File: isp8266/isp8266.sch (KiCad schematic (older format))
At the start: 61 parts, among them J1 S0, J10 F1, J2 S2, J3 S1, J4 S3, J5 IMU, J6 USART, J7 F0, J8 BATTERY, J9 I2C, Q1 S8050, Q2 S8050, Q3 IRLML0030, Q4 IRLML0030, SW1 SW_Push, U1 CH340C, U2 AP1117-33, U3 IPS5306, U4 ESP-12E

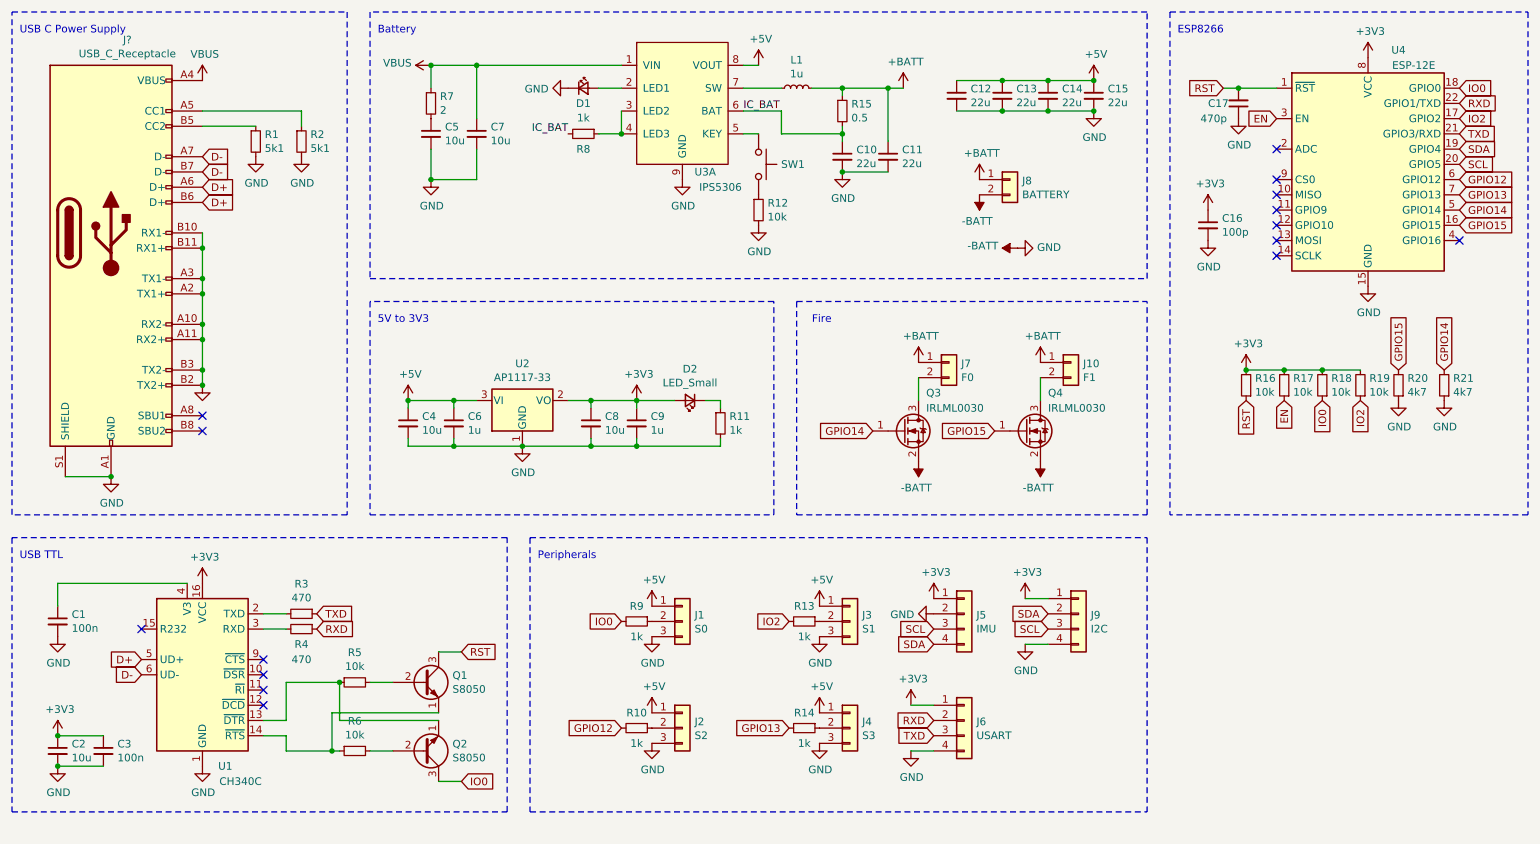
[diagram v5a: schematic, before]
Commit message: Add rst button and footprint
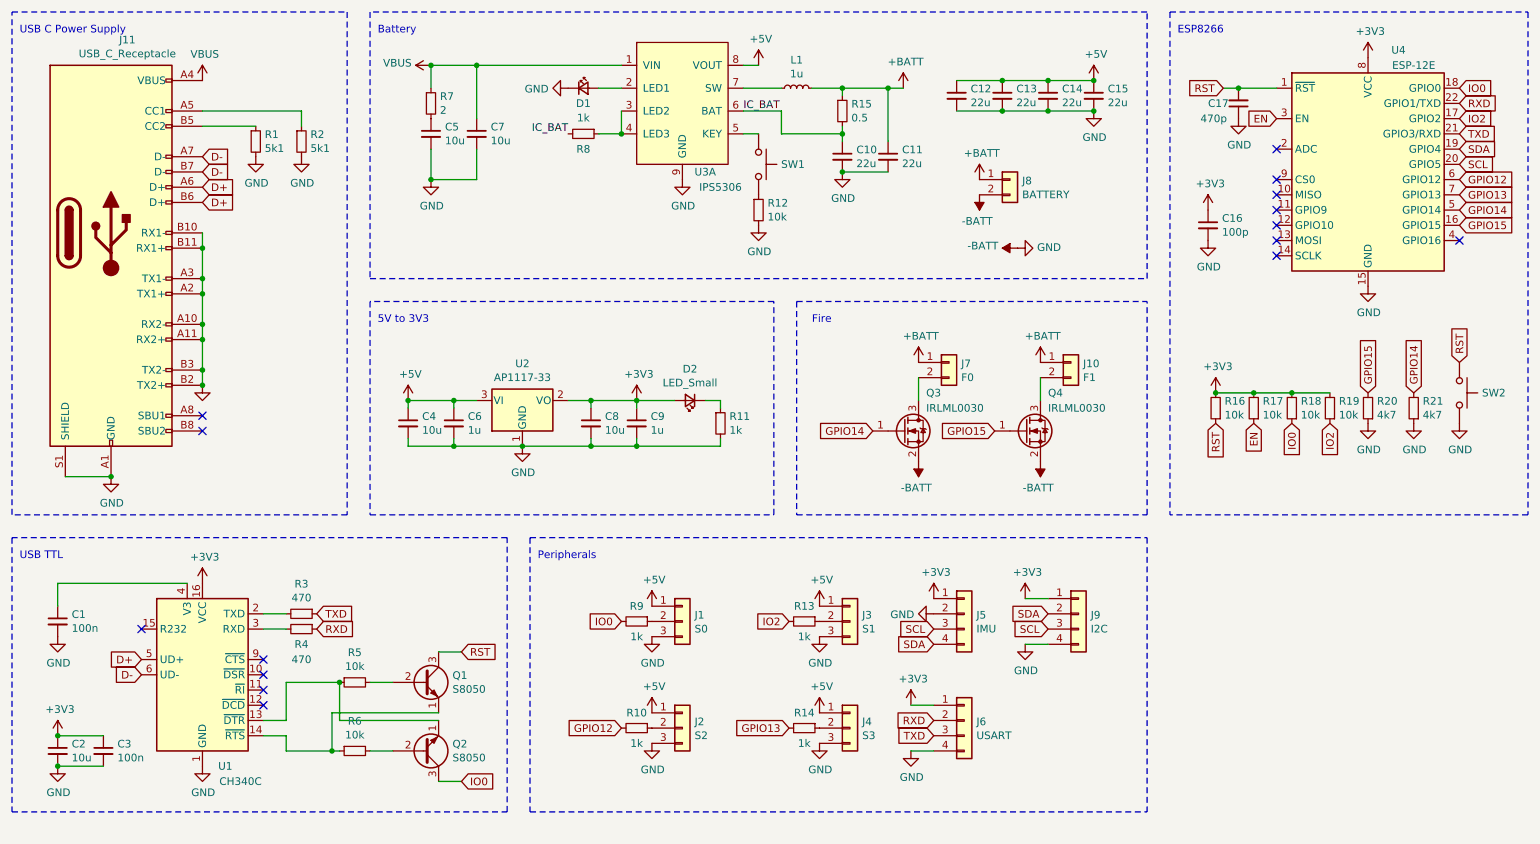
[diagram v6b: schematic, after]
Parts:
- added SW2: SW_Push, symbol Switch:SW_Push
- C1, C10, C11, C12, C13, C14, C15, C16, C17, C2, C3, C4, C5, C6, C7, C8, C9: footprint (none) -> Capacitor_SMD:C_0603_1608Metric
- D1, D2: footprint (none) -> LED_SMD:LED_0603_1608Metric
- J1, J2, J3, J4: footprint (none) -> Connector_PinSocket_2.54mm:PinSocket_1x03_P2.54mm_Vertical
- J11: renamed from J?; footprint (none) -> Connector_USB:USB_C_Receptacle_Amphenol_12401610E4-2A
- J5, J6: footprint (none) -> Connector_PinSocket_2.54mm:PinSocket_1x04_P2.54mm_Vertical
- J8: footprint (none) -> Connector_Molex:Molex_KK-254_AE-6410-02A_1x02_P2.54mm_Vertical
- J9: footprint (none) -> Connector_PinSocket_2.54mm:PinSocket_1x04_P2.54mm_Horizontal
- L1: footprint (none) -> Inductor_SMD:L_Abracon_ASPI-0630LR
- R1, R10, R11, R12, R13, R14, R15, R16, R17, R18, R19, R2, R20, R21, R3, R4, R5, R6, R7, R8, R9: footprint (none) -> Resistor_SMD:R_0603_1608Metric
- U3: footprint (none) -> Package_SO:HTSOP-8-1EP_3.9x4.9mm_P1.27mm_EP2.4x3.2mm
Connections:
- net -BATT: now also SW2.2
- net RST: now also SW2.1
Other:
- moved on the sheet: R16, R17, R18, R19, R20, R21

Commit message: Typo
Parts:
- removed U3: IPS5306, Package_SO:HTSOP-8-1EP_3.9x4.9mm_P1.27mm_EP2.4x3.2mm, symbol IPS5306:IPS5306
- added U3: IP5306, symbol IP5306:IP5306
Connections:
- net +5V: now also U3.8 (VOUT)
- net -BATT: now also U3.9 (GND)
- net IC_BAT: now also U3.6 (BAT)
- net VBUS: now also U3.1 (VIN)
- net at D1.2 (A): now also U3.2 (LED1)
- net at R8.1: now also U3.3 (LED2), U3.4 (LED3)
- net at SW1.1: now also U3.5 (KEY)
- net at L1.1: now also U3.7 (SW)
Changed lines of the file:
@@
 	1    0    0    -1
 $EndComp
-Connection ~ 4650 1400
 Wire Wire Line
 	4650 1250 4650 1400
@@
 F 3 "" H 5050 1700 50  0001 C CNN
 	1    5050 1700
-	1    0    0    -1
-$EndComp
-$Comp
-L IPS5306:IPS5306 U3
-U 1 1 637F6934
-P 5050 1200
-F 0 "U3" H 5200 750 50  0000 C CNN
-F 1 "IPS5306" H 5300 650 50  0000 C CNN
-F 2 "Package_SO:HTSOP-8-1EP_3.9x4.9mm_P1.27mm_EP2.4x3.2mm" H 5050 1200 50  0001 C CNN
-F 3 "" H 5050 1200 50  0001 C CNN
-	1    5050 1200
 	1    0    0    -1
 $EndComp
@@
 	-1   0    0    1
 $EndComp
+$Comp
+L IP5306:IP5306 U3
+U 1 1 63811B86
+P 5050 1200
+F 0 "U3" H 5200 750 50  0000 C CNN
+F 1 "IP5306" H 5250 650 50  0000 C CNN
+F 2 "" H 5050 1200 50  0001 C CNN
+F 3 "" H 5050 1200 50  0001 C CNN
+	1    5050 1200
+	1    0    0    -1
+$EndComp
+Connection ~ 4650 1400
 $EndSCHEMATC

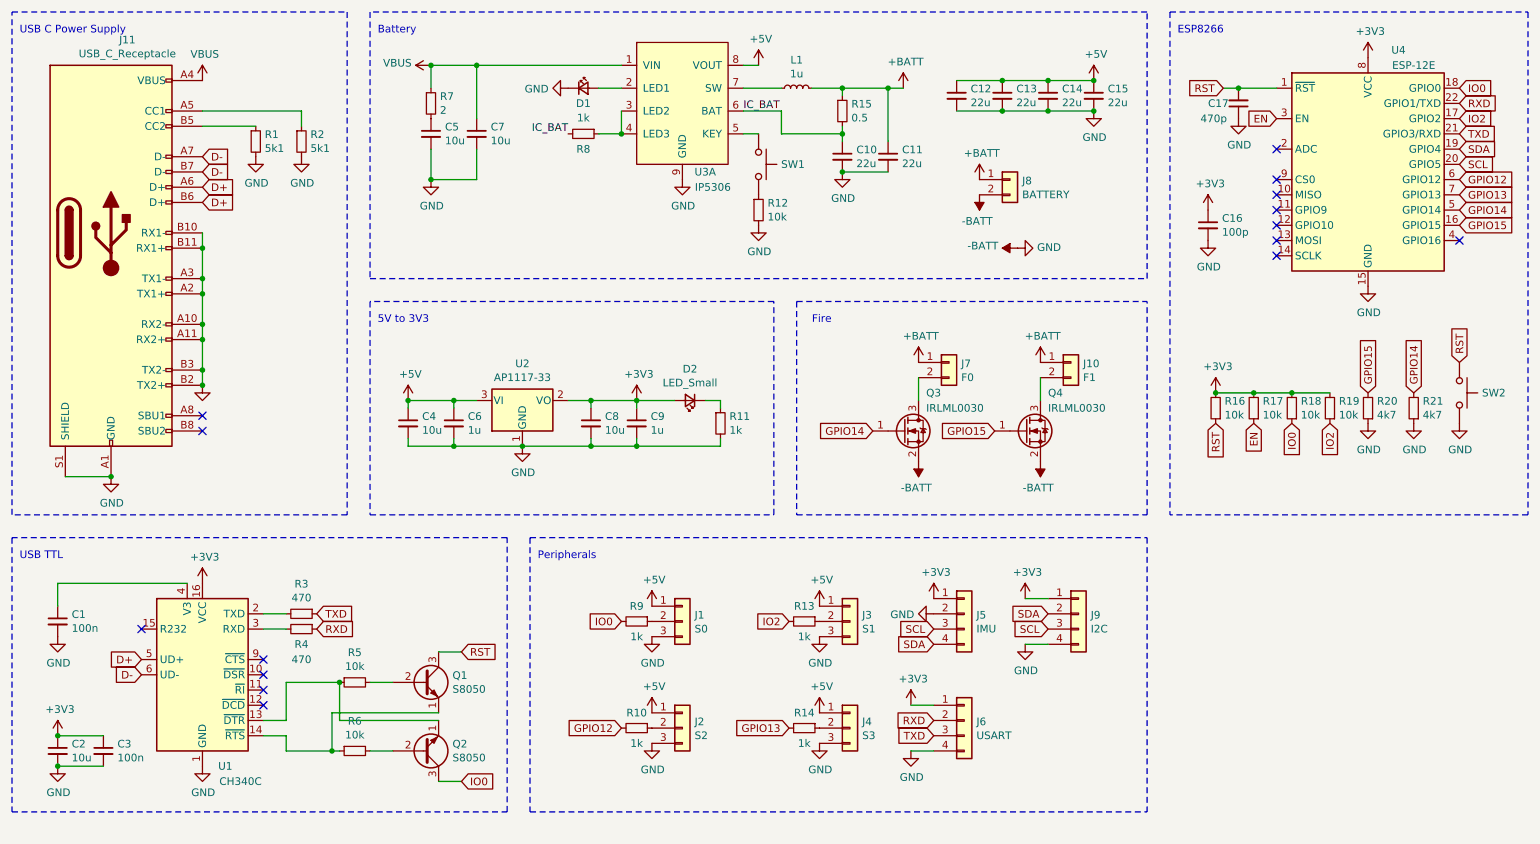
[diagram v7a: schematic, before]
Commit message: Change ignition circuits
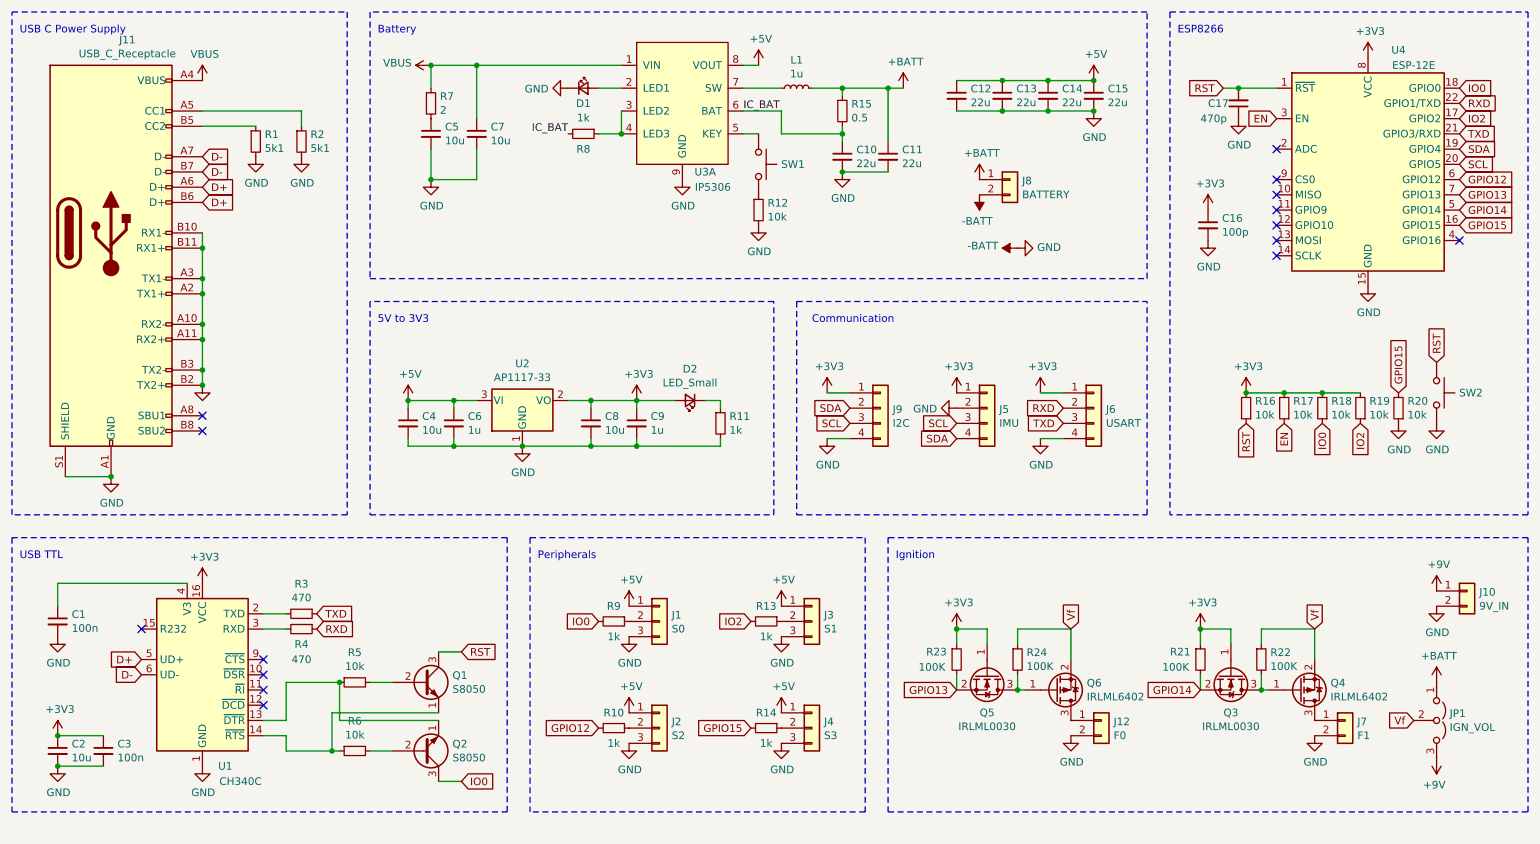
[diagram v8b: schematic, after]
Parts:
- removed Q4: IRLML0030, Package_TO_SOT_SMD:SOT-23, symbol Transistor_FET:IRLML0030
- added J12: F0, symbol Connector_Generic:Conn_01x02
- added JP1: IGN_VOL, symbol Jumper:Jumper_3_Open
- added Q4, Q6: IRLML6402, Package_TO_SOT_SMD:SOT-23, symbol Transistor_FET:IRLML6402
- added Q5: IRLML0030, Package_TO_SOT_SMD:SOT-23, symbol Transistor_FET:IRLML0030
- added R22, R23, R24: 100K, symbol Device:R_Small
- J10: value F1 -> 9V_IN
- J7: value F0 -> F1
- R20: value 4k7 -> 10k
- R21: value 4k7 -> 100K; footprint Resistor_SMD:R_0603_1608Metric -> (none)
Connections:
- net +3V3: now also Q3.1 (G), R21.1, Q5.1 (G), R23.1
- net +BATT: now also JP1.1 (A); no longer J10.1 (Pin_1), J7.1 (Pin_1)
- net -BATT: now also J10.2 (Pin_2), J7.2 (Pin_2), J12.2 (Pin_2); no longer Q3.2 (S), R21.1
- net GPIO13: now also Q5.2 (S), R23.2; no longer R14.2
- net GPIO14: now also Q3.2 (S); no longer Q3.1 (G)
- net GPIO15: now also R14.2
- net at Q3.3 (D): now also Q4.1 (G), R22.2; no longer J7.2 (Pin_2)
- new net: Q5.3 (D), Q6.1 (G), R24.2
- new net: J12.1 (Pin_1), Q6.3 (D)
- new net: J7.1 (Pin_1), Q4.3 (D)
- new net +9V: J10.1 (Pin_1), JP1.3 (B)
- new net Vf: JP1.2 (C), Q4.2 (S), Q6.2 (S), R22.1, R24.1
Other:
- note added: "Communication"
- note added: "Ignition"
- note removed: "Fire"
- moved on the sheet: J1, J2, J3, J4, J5, J6, J9, R10, R13, R14, R16, R17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
